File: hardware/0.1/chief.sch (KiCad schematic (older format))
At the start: 26 parts, among them J1 USB_C_Receptacle_USB2.0, SW1 Encoder_MX_RGB, SW10 Encoder_MX_RGB, SW11 MX_RGB, SW12 MX_RGB, SW2 MX_RGB, SW3 MX_RGB, SW4 Encoder_MX_RGB, SW5 MX_RGB, SW6 MX_RGB, SW7 Encoder_MX_RGB, SW8 MX_RGB, SW9 MX_RGB, U1 AP2112K-3.3, U2 USBLC6-2SC6, U3 STM32F072C8Tx

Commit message: Update schematics
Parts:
- removed RN1: 5K1, symbol josh-passive:RN
- added BZ1: Buzzer, Buzzer_Beeper:Buzzer_Murata_PKMCS0909E4000-R1, symbol Device:Buzzer
- added C10, C11, C12, C13, C14, C15, C6, C7, C8, C9: 100n, Capacitor_SMD:C_0603_1608Metric, symbol Device:C
- added C4: 4u7, Capacitor_SMD:C_0603_1608Metric, symbol Device:C
- added C5: 10u, Capacitor_SMD:C_0603_1608Metric, symbol Device:C
- added D1: 1N4148, Diode_THT:D_DO-35_SOD27_P7.62mm_Horizontal, symbol Diode:1N4148
- added D2: LED, LED_SMD:LED_0603_1608Metric, symbol Device:LED
- added Q1: DTC123J, Package_TO_SOT_SMD:SOT-23, symbol Transistor_BJT:DTC123J
- added Q2: BSS138, Package_TO_SOT_SMD:SOT-23, symbol Transistor_FET:BSS138
- added R1: 1K5, Resistor_SMD:R_0603_1608Metric, symbol Device:R
- added R2: 100K, Resistor_SMD:R_0603_1608Metric, symbol Device:R
- added R3, R4: 10K, Resistor_SMD:R_0603_1608Metric, symbol Device:R
- added R5: 2K2, Resistor_SMD:R_0603_1608Metric, symbol Device:R
- added RN1, RN2, RN3, RN4: 10K, Resistor_SMD:R_Array_Concave_4x0603, symbol chief-rescue:RN-josh-passive
- added RN5: 5K1, Resistor_SMD:R_Array_Concave_4x0603, symbol chief-rescue:RN-josh-passive
- added SW13: SW_Push, symbol Switch:SW_Push
- C1, C2, C3: footprint (none) -> Capacitor_SMD:C_0603_1608Metric
- FB1: symbol josh-passive:Ferrite_Bead_PWR -> chief-rescue:Ferrite_Bead_PWR-josh-passive
- SW1, SW10, SW4, SW7: symbol josh-keyboard:Encoder_MX_RGB -> chief-rescue:Encoder_MX_RGB-josh-keyboard
- SW11, SW12, SW2, SW3, SW5, SW6, SW8, SW9: symbol josh-keyboard:MX_RGB -> chief-rescue:MX_RGB-josh-keyboard
- U2: symbol josh-ic:USBLC6-2SC6 -> chief-rescue:USBLC6-2SC6-josh-ic
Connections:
- net labels added: +3.3V, BOOT0, BUZZER, ENC1A_DB, ENC1B_DB, ENC2A_DB, ENC2B_DB, ENC3A_DB, ENC3B_DB, ENC4A_DB, ENC4B_DB, LED, PA0, PA1, PA10, PA11, PA12, PA13, PA14, PA15, PA2, PA3, PA4, PA5, PA6, PA7, PA8, PA9, PB0, PB1, PB10, PB11, PB12, PB13, PB14, PB15, PB2, PB3, PB4, PB5, PB6, PB7, PB8, PB9, nRST
- wire segments 144 -> 300
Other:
- note added: "Alicia Keys"
- note added: "Audio"
- note added: "Debounce"
- note added: "Microcontroller"
- note added: "Power\nIndicator"
- note added: "Reset"
- note added: "Step Up\n"
- note added: "USB Type-C Connector"
- note added: "Voltage Regulator"
- moved on the sheet: C1, C2, C3, F1, H1, H2, H3, H4, J1, U1, U3

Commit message: Associate footprints
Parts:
- J1: footprint (none) -> josh-connectors:USB_C_U262-161N-4BVC11
- SW13: footprint (none) -> josh-buttons-switches:Panasonic_EVQPUL_EVQPUC
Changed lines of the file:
@@
 F 0 "J1" H 1107 2817 50  0000 C CNN
 F 1 "USB_C_Receptacle_USB2.0" H 1107 2726 50  0000 C CNN
-F 2 "" H 1150 1950 50  0001 C CNN
+F 2 "josh-connectors:USB_C_U262-161N-4BVC11" H 1150 1950 50  0001 C CNN
 F 3 "https://www.usb.org/sites/default/files/documents/usb_type-c.zip" H 1150 1950 50  0001 C CNN
 	1    1000 1950
@@
 F 0 "SW13" H 950 6150 50  0000 C CNN
 F 1 "SW_Push" H 950 5850 50  0000 C CNN
-F 2 "" H 950 6150 50  0001 C CNN
+F 2 "josh-buttons-switches:Panasonic_EVQPUL_EVQPUC" H 950 6150 50  0001 C CNN
 F 3 "~" H 950 6150 50  0001 C CNN
 	1    950  5950

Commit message: parts ready to layout
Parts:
- added JP1: Jumper_NC_Small, Jumper:SolderJumper-2_P1.3mm_Bridged_RoundedPad1.0x1.5mm, symbol Device:Jumper_NC_Small
- D1: footprint Diode_THT:D_DO-35_SOD27_P7.62mm_Horizontal -> Diode_SMD:D_SOD-123
- F1: footprint josh-passives-smt:Fuse_0805_2012Metric -> josh-passives-smt:Fuse_0603_1608Metric
- R1: value 1K5 -> 2K2
- RN1, RN2, RN3, RN4, RN5: footprint Resistor_SMD:R_Array_Concave_4x0603 -> Resistor_SMD:R_Array_Convex_4x0603
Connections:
- net +3V3: now also JP1.1; no longer R5.1
- net +5V: now also C1.1, R4.1, U1.1 (VIN), U1.3 (EN)
- net BOOT0: now also C5.1, D1.1 (K), R2.1
- net BUZZER: now also U3.14 (PA4)
- net VBUS: no longer C1.1, R4.1, U1.1 (VIN), U1.3 (EN)
- new net: JP1.2, R5.1
- no-connect marks 3 -> 4
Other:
- moved on the sheet: C5

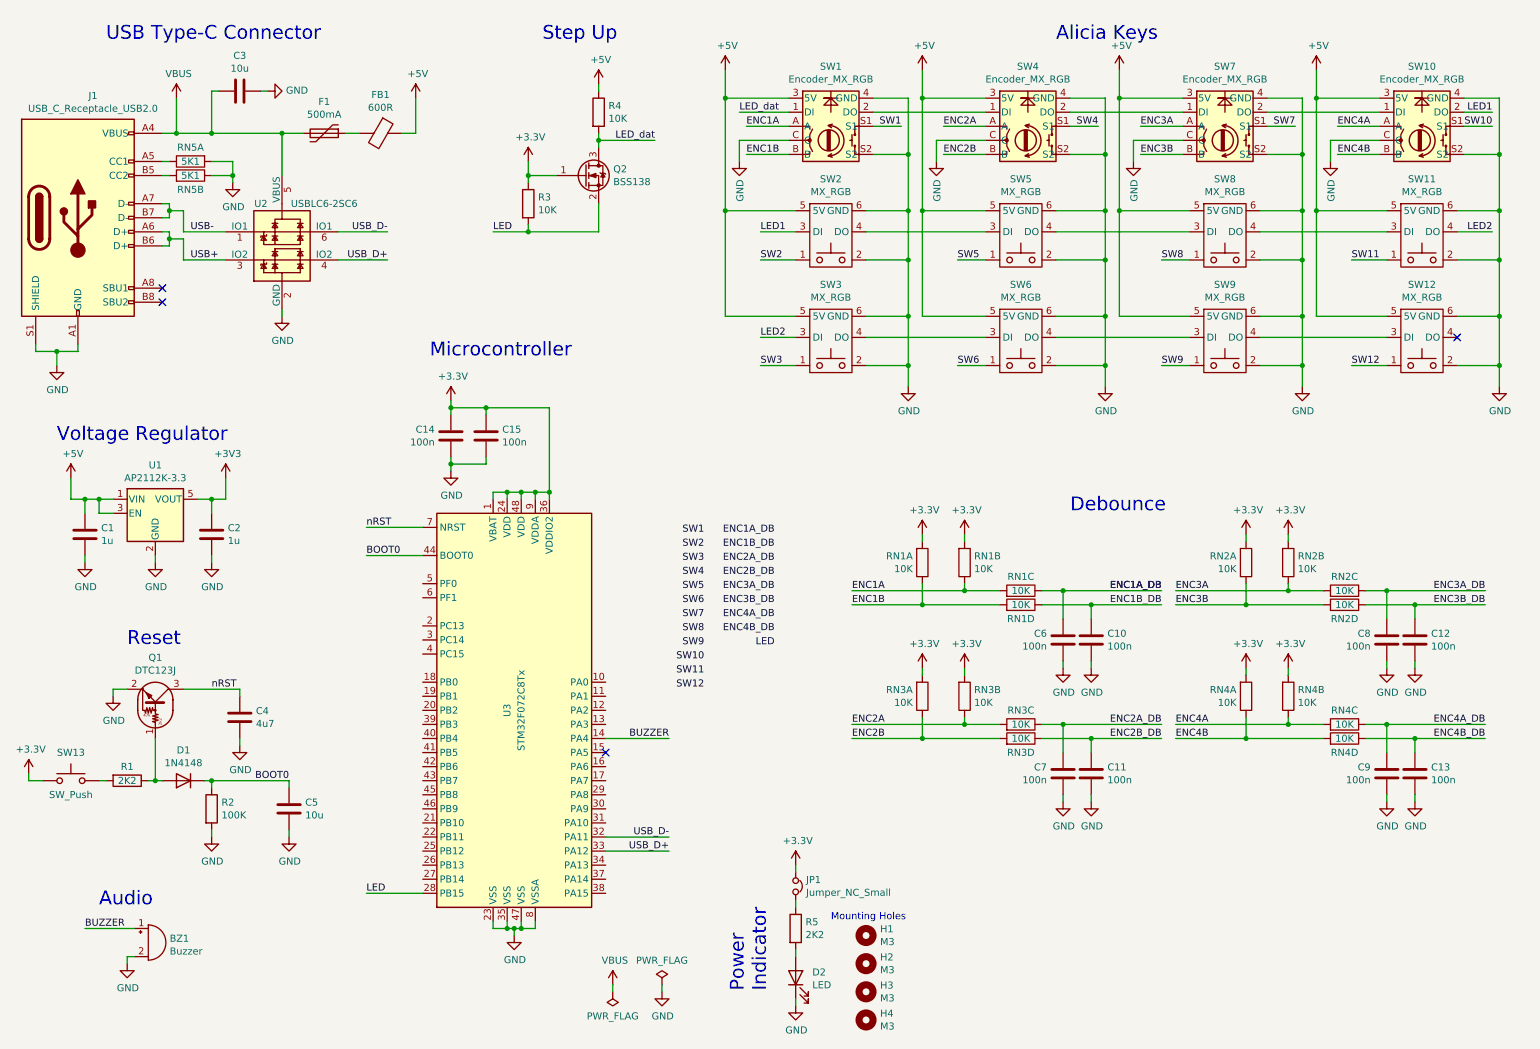
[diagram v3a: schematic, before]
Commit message: Layout complete. ENC2/ENC2DB swapped with ENC3/ENC3DB to match resistor labelling
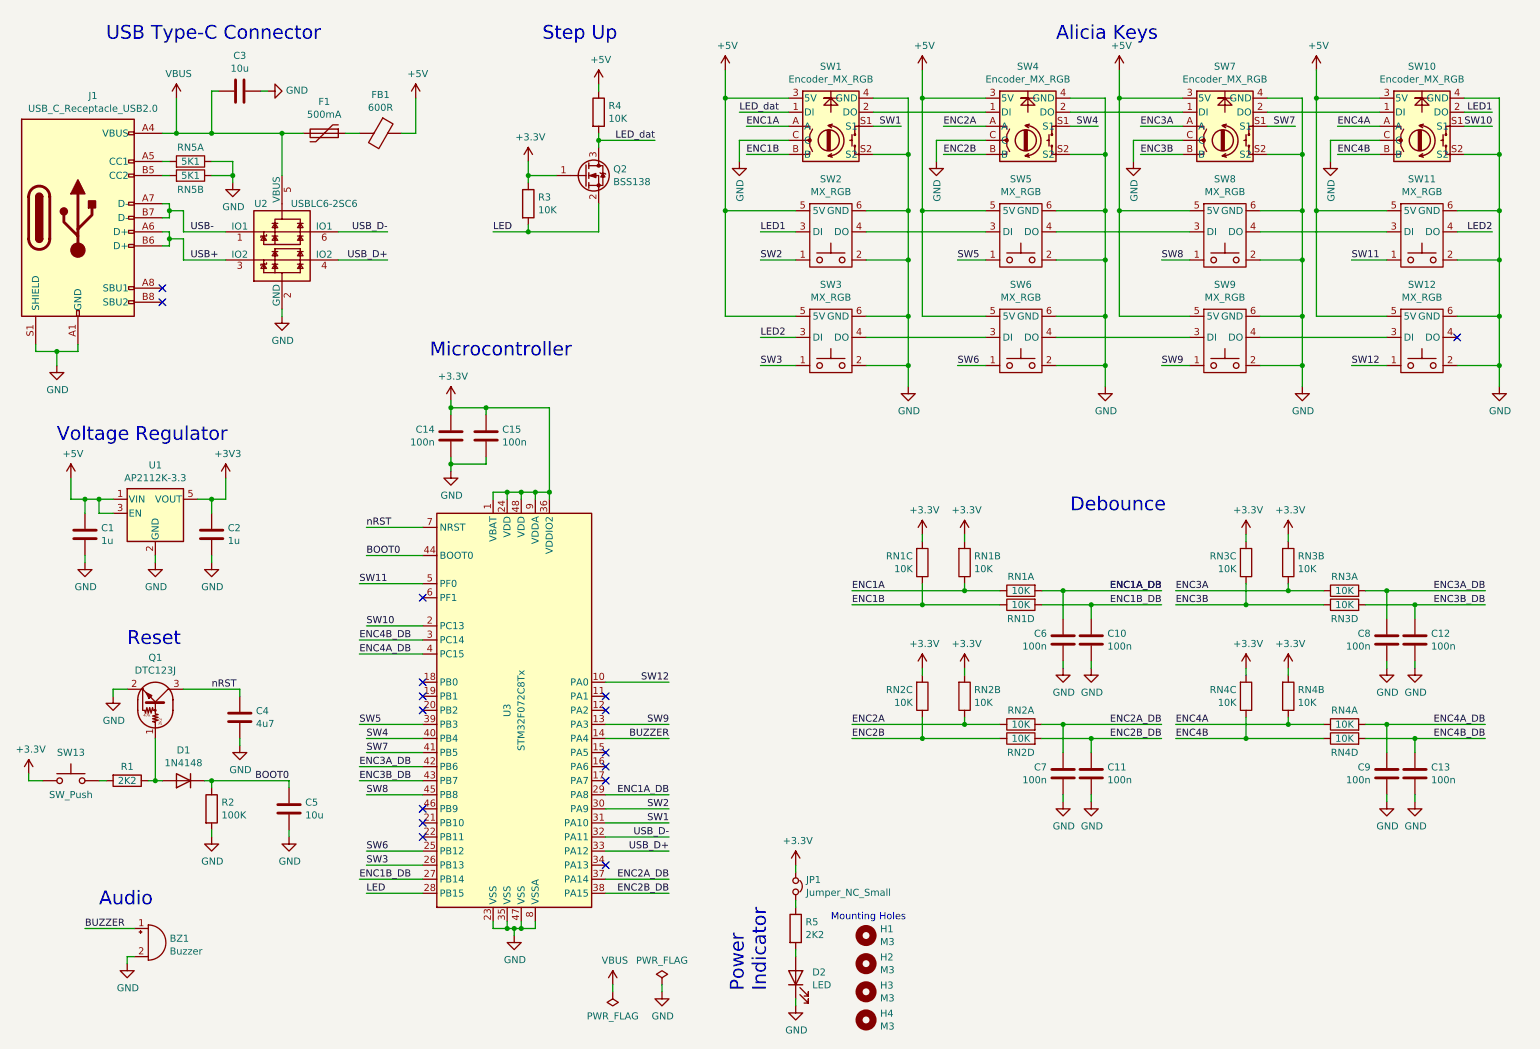
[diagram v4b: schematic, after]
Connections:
- net +3V3: now also RN1.2, RN2.2, RN3.2, RN4.2; no longer RN1.4, RN2.4, RN3.4, RN4.4
- net ENC1A: now also RN1.5; no longer RN1.2
- net ENC1A_DB: now also RN1.4, U3.29 (PA8); no longer RN1.7
- net ENC1B: now also RN1.7, RN1.8; no longer RN1.1, RN1.5
- net ENC1B_DB: now also RN1.1, U3.27 (PB14); no longer RN1.8
- net ENC2A: now also RN2.5, RN2.6; no longer RN3.2, RN3.6
- net ENC2A_DB: now also RN2.4, U3.37 (PA14); no longer RN3.7
- net ENC2B: now also RN2.7, RN2.8; no longer RN3.1, RN3.5
- net ENC2B_DB: now also RN2.1, U3.38 (PA15); no longer RN3.8
- net ENC3A: now also RN3.5, RN3.6; no longer RN2.2, RN2.6
- net ENC3A_DB: now also RN3.4, U3.42 (PB6); no longer RN2.7
- net ENC3B: now also RN3.7, RN3.8; no longer RN2.1, RN2.5
- net ENC3B_DB: now also RN3.1, U3.43 (PB7); no longer RN2.8
- net ENC4A: now also RN4.5; no longer RN4.2
- net ENC4A_DB: now also RN4.4, U3.4 (PC15); no longer RN4.7
- net ENC4B: now also RN4.7, RN4.8; no longer RN4.1, RN4.5
- net ENC4B_DB: now also RN4.1, U3.3 (PC14); no longer RN4.8
- net GND: now also RN5.5; no longer RN5.4
- net SW1: now also U3.31 (PA10)
- net SW10: now also U3.2 (PC13)
- net SW11: now also U3.5 (PF0)
- net SW12: now also U3.10 (PA0)
- net SW2: now also U3.30 (PA9)
- net SW3: now also U3.26 (PB13)
- net SW4: now also U3.40 (PB4)
- net SW5: now also U3.39 (PB3)
- net SW6: now also U3.25 (PB12)
- net SW7: now also U3.41 (PB5)
- net SW8: now also U3.45 (PB8)
- net SW9: now also U3.13 (PA3)
- net at J1.A5 (CC1): now also RN5.4; no longer RN5.5
- no-connect marks 4 -> 16
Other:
- moved on the sheet: RN2B, RN2D, RN3B, RN3D

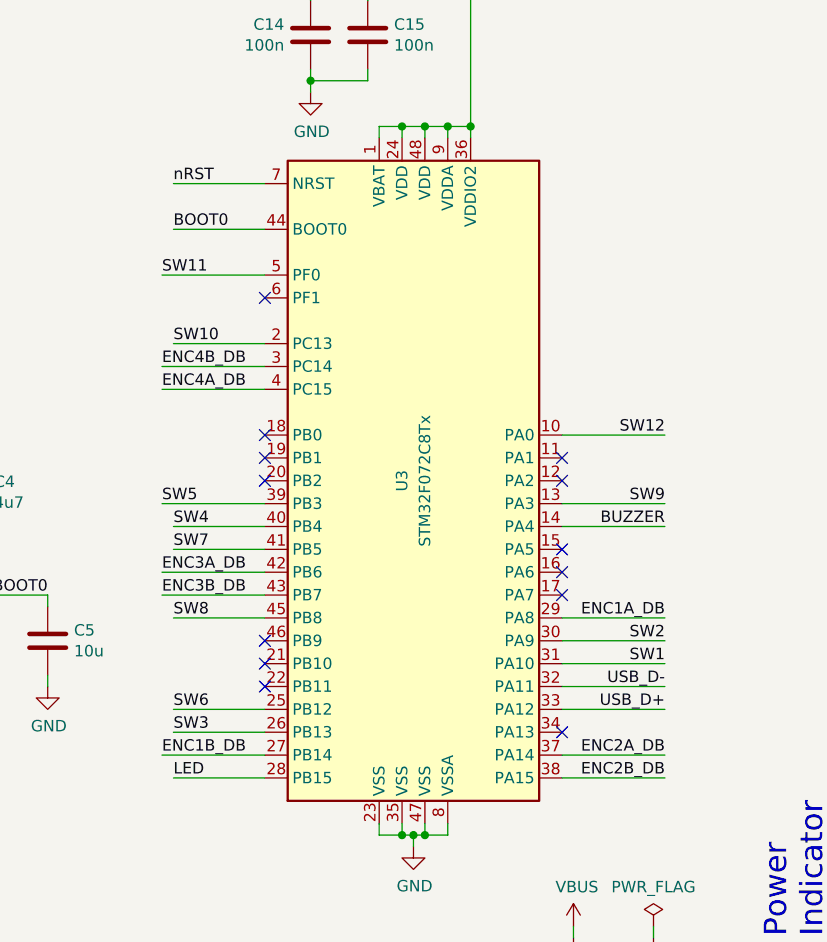
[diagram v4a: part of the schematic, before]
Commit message: Footprints arranged and layout attempted
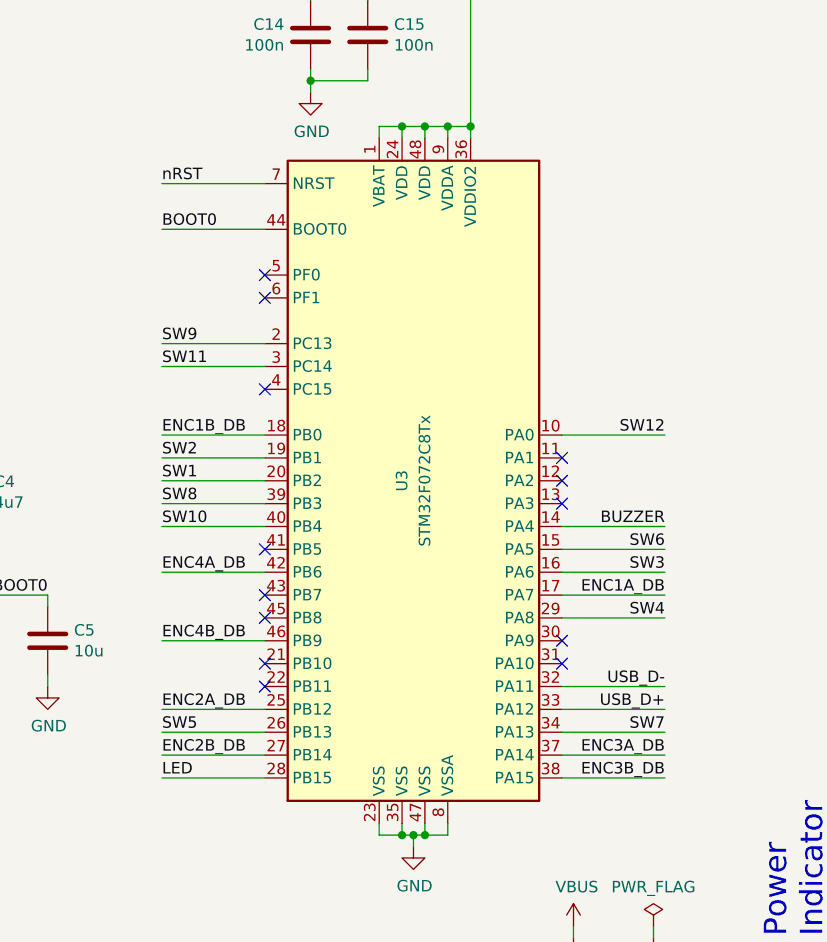
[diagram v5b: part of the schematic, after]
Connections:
- net ENC1A_DB: now also U3.17 (PA7); no longer U3.29 (PA8)
- net ENC1B_DB: now also U3.18 (PB0); no longer U3.27 (PB14)
- net ENC2A_DB: now also U3.25 (PB12); no longer U3.37 (PA14)
- net ENC2B_DB: now also U3.27 (PB14); no longer U3.38 (PA15)
- net ENC3A_DB: now also U3.37 (PA14); no longer U3.42 (PB6)
- net ENC3B_DB: now also U3.38 (PA15); no longer U3.43 (PB7)
- net ENC4A_DB: now also U3.42 (PB6); no longer U3.4 (PC15)
- net ENC4B_DB: now also U3.46 (PB9); no longer U3.3 (PC14)
- net SW1: now also U3.20 (PB2); no longer U3.31 (PA10)
- net SW10: now also U3.40 (PB4); no longer U3.2 (PC13)
- net SW11: now also U3.3 (PC14); no longer U3.5 (PF0)
- net SW2: now also U3.19 (PB1); no longer U3.30 (PA9)
- net SW3: now also U3.16 (PA6); no longer U3.26 (PB13)
- net SW4: now also U3.29 (PA8); no longer U3.40 (PB4)
- net SW5: now also U3.26 (PB13); no longer U3.39 (PB3)
- net SW6: now also U3.15 (PA5); no longer U3.25 (PB12)
- net SW7: now also U3.34 (PA13); no longer U3.41 (PB5)
- net SW8: now also U3.39 (PB3); no longer U3.45 (PB8)
- net SW9: now also U3.2 (PC13); no longer U3.13 (PA3)
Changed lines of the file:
@@
 Wire Wire Line
 	2450 2650 2450 2600
-$Comp
-L MCU_ST_STM32F0:STM32F072C8Tx U3
-U 1 1 5EFC05F6
-P 4150 5450
-F 0 "U3" V 4050 5450 50  0000 C CNN
-F 1 "STM32F072C8Tx" V 4150 5450 50  0000 C CNN
-F 2 "Package_QFP:LQFP-48_7x7mm_P0.5mm" H 3550 4050 50  0001 R CNN
-F 3 "http://www.st.com/st-web-ui/static/active/en/resource/technical/document/datasheet/DM00090510.pdf" H 4150 5450 50  0001 C CNN
-	1    4150 5450
-	1    0    0    -1
-$EndComp
 Wire Wire Line
 	10850 1100 11100 1100
@@
 Wire Wire Line
 	4100 7000 4150 7000
-Text Label 3050 6750 0    50   ~ 0
+Text Label 3000 6750 0    50   ~ 0
 LED
 Wire Wire Line
-	3450 6750 3050 6750
+	3450 6750 3000 6750
 $Comp
 L chief-rescue:RN-josh-passive RN3
@@
 Text Label 1950 5300 0    50   ~ 0
 nRST
-Text Label 3050 4150 0    50   ~ 0
+Text Label 3000 4150 0    50   ~ 0
 nRST
 Wire Wire Line
-	3050 4150 3450 4150
-Text Label 3050 4350 0    50   ~ 0
+	3000 4150 3450 4150
+Text Label 3000 4350 0    50   ~ 0
 BOOT0
 Wire Wire Line
-	3050 4350 3450 4350
+	3000 4350 3450 4350
 Text Label 5200 6350 2    50   ~ 0
 USB_D-
@@
 Text Label 8700 4600 2    50   ~ 0
 ENC1A_DB
-Text Label 5200 6050 2    50   ~ 0
+Text Label 5200 5950 2    50   ~ 0
 ENC1A_DB
-Text Label 3000 6650 0    50   ~ 0
-ENC1B_DB
+Text Label 3000 6150 0    50   ~ 0
+ENC4B_DB
+Text Label 3000 5850 0    50   ~ 0
+ENC4A_DB
 Text Label 5200 6650 2    50   ~ 0
-ENC2A_DB
+ENC3A_DB
 Text Label 5200 6750 2    50   ~ 0
-ENC2B_DB
-Text Label 3000 4950 0    50   ~ 0
-ENC4B_DB
-Text Label 3000 5050 0    50   ~ 0
-ENC4A_DB
-Text Label 3000 5850 0    50   ~ 0
-ENC3A_DB
-Text Label 3000 5950 0    50   ~ 0
 ENC3B_DB
 Text Label 5200 5650 2    50   ~ 0
 BUZZER
-Text Label 5200 6250 2    50   ~ 0
+Text Label 3000 5450 0    50   ~ 0
 SW1
-Text Label 5200 6150 2    50   ~ 0
+Text Label 3000 5350 0    50   ~ 0
 SW2
-Text Label 3050 6450 0    50   ~ 0
+Text Label 5200 5750 2    50   ~ 0
 SW6
-Text Label 3050 5750 0    50   ~ 0
+Text Label 5200 6550 2    50   ~ 0
 SW7
-Text Label 3050 6050 0    50   ~ 0
-SW8
-Text Label 5200 5550 2    50   ~ 0
+Text Label 3000 4850 0    50   ~ 0
 SW9
-Text Label 3050 4850 0    50   ~ 0
+Text Label 3000 5650 0    50   ~ 0
 SW10
 Wire Wire Line
 	5200 5650 4750 5650
-NoConn ~ 4750 5750
 $Comp
 L chief-rescue:RN-josh-passive RN3
@@
 $EndComp
 Wire Wire Line
-	4750 6250 5200 6250
+	3450 5450 3000 5450
 $Comp
 L chief-rescue:RN-josh-passive RN2
@@
 $EndComp
 Wire Wire Line
-	3050 6050 3450 6050
-Wire Wire Line
-	5200 6150 4750 6150
-Wire Wire Line
-	4750 5550 5200 5550
+	3000 5350 3450 5350
+Wire Wire Line
+	3450 4850 3000 4850
 Text Label 5200 5250 2    50   ~ 0
 SW12
@@
 	4750 5250 5200 5250
 Wire Wire Line
-	3050 6450 3450 6450
+	5200 5750 4750 5750
 $Comp
 L chief-rescue:RN-josh-passive RN1
@@
 $EndComp
 Wire Wire Line
-	3450 6650 3000 6650
-Wire Wire Line
-	4750 6050 5200 6050
-Text Label 3050 6550 0    50   ~ 0
+	4750 5950 5200 5950
+Wire Wire Line
+	5200 6050 4750 6050
+Text Label 5200 6050 2    50   ~ 0
+SW4
+Wire Wire Line
+	5200 6550 4750 6550
+Wire Wire Line
+	5200 6750 4750 6750
+Wire Wire Line
+	5200 6650 4750 6650
+Wire Wire Line
+	3000 5650 3450 5650
+Wire Wire Line
+	3000 6150 3450 6150
+Wire Wire Line
+	3000 5850 3450 5850
+Wire Wire Line
+	3450 4950 3000 4950
+Text Label 3000 4950 0    50   ~ 0
+SW11
+Text Label 5200 5850 2    50   ~ 0
 SW3
 Wire Wire Line
-	3050 6550 3450 6550
-Wire Wire Line
-	4750 6650 5200 6650
-Wire Wire Line
-	5200 6750 4750 6750
-Wire Wire Line
-	3050 5650 3450 5650
-Wire Wire Line
-	3450 5550 3000 5550
+	5200 5850 4750 5850
+Wire Wire Line
+	3450 5250 3000 5250
+Text Label 3000 5250 0    50   ~ 0
+ENC1B_DB
+Wire Wire Line
+	3000 6650 3450 6650
+Wire Wire Line
+	3450 6450 3000 6450
+Text Label 3000 6650 0    50   ~ 0
+ENC2B_DB
+Text Label 3000 6450 0    50   ~ 0
+ENC2A_DB
+$Comp
+L MCU_ST_STM32F0:STM32F072C8Tx U3
+U 1 1 5EFC05F6
+P 4150 5450
+F 0 "U3" V 4050 5450 50  0000 C CNN
+F 1 "STM32F072C8Tx" V 4150 5450 50  0000 C CNN
+F 2 "Package_QFP:LQFP-48_7x7mm_P0.5mm" H 3550 4050 50  0001 R CNN
+F 3 "http://www.st.com/st-web-ui/static/active/en/resource/technical/document/datasheet/DM00090510.pdf" H 4150 5450 50  0001 C CNN
+	1    4150 5450
+	1    0    0    -1
+$EndComp
+Text Label 3000 6550 0    50   ~ 0
+SW5
+Wire Wire Line
+	3450 6550 3000 6550
+Wire Wire Line
+	3000 5550 3450 5550
 Text Label 3000 5550 0    50   ~ 0
-SW5
-Text Label 3050 5650 0    50   ~ 0
-SW4
-Wire Wire Line
-	3050 5750 3450 5750
-Wire Wire Line
-	3000 5950 3450 5950
-Wire Wire Line
-	3000 5850 3450 5850
-Wire Wire Line
-	3050 4850 3450 4850
-Wire Wire Line
-	3000 4950 3450 4950
-Wire Wire Line
-	3000 5050 3450 5050
-Wire Wire Line
-	3450 4550 3000 4550
-Text Label 3000 4550 0    50   ~ 0
-SW11
+SW8
+NoConn ~ 3450 4550
 NoConn ~ 3450 4650
-NoConn ~ 3450 5250
-NoConn ~ 3450 5350
-NoConn ~ 3450 5450
+NoConn ~ 3450 5050
+NoConn ~ 3450 5750
+NoConn ~ 3450 5950
+NoConn ~ 3450 6050
+NoConn ~ 3450 6250
+NoConn ~ 3450 6350
+NoConn ~ 4750 6150
+NoConn ~ 4750 6250
+NoConn ~ 4750 5550
+NoConn ~ 4750 5450
 NoConn ~ 4750 5350
-NoConn ~ 4750 5450
-NoConn ~ 4750 5850
-NoConn ~ 4750 5950
-NoConn ~ 4750 6550
-NoConn ~ 3450 6350
-NoConn ~ 3450 6250
-NoConn ~ 3450 6150
 $EndSCHEMATC
